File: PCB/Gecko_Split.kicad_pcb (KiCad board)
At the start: 2 copper layers, 142.5 x 106.3 mm, 83 parts, among them J1 LED, J2 4PIN, J3 OLED, P1 i2c_pin, P2 i2c_pin, SW1 SW_PUSH, SW10 SW_PUSH, SW11 SW_PUSH, SW12 SW_PUSH, SW13 SW_PUSH, SW14 SW_PUSH, SW15 SW_PUSH, SW16 SW_PUSH, SW17 SW_PUSH, SW18 SW_PUSH, SW19 SW_PUSH, SW2 SW_PUSH, SW20 SW_PUSH, SW21 SW_PUSH, SW22 SW_PUSH, SW23 SW_PUSH, SW24 SW_PUSH, SW25 SW_PUSH, SW26 SW_PUSH, SW27 SW_PUSH, SW28 SW_PUSH, SW29 SW_PUSH, SW3 SW_PUSH, SW4 SW_PUSH, SW5 SW_PUSH, SW6 SW_PUSH, SW7 SW_PUSH, SW8 SW_PUSH, SW9 SW_PUSH, U1 ProMicro

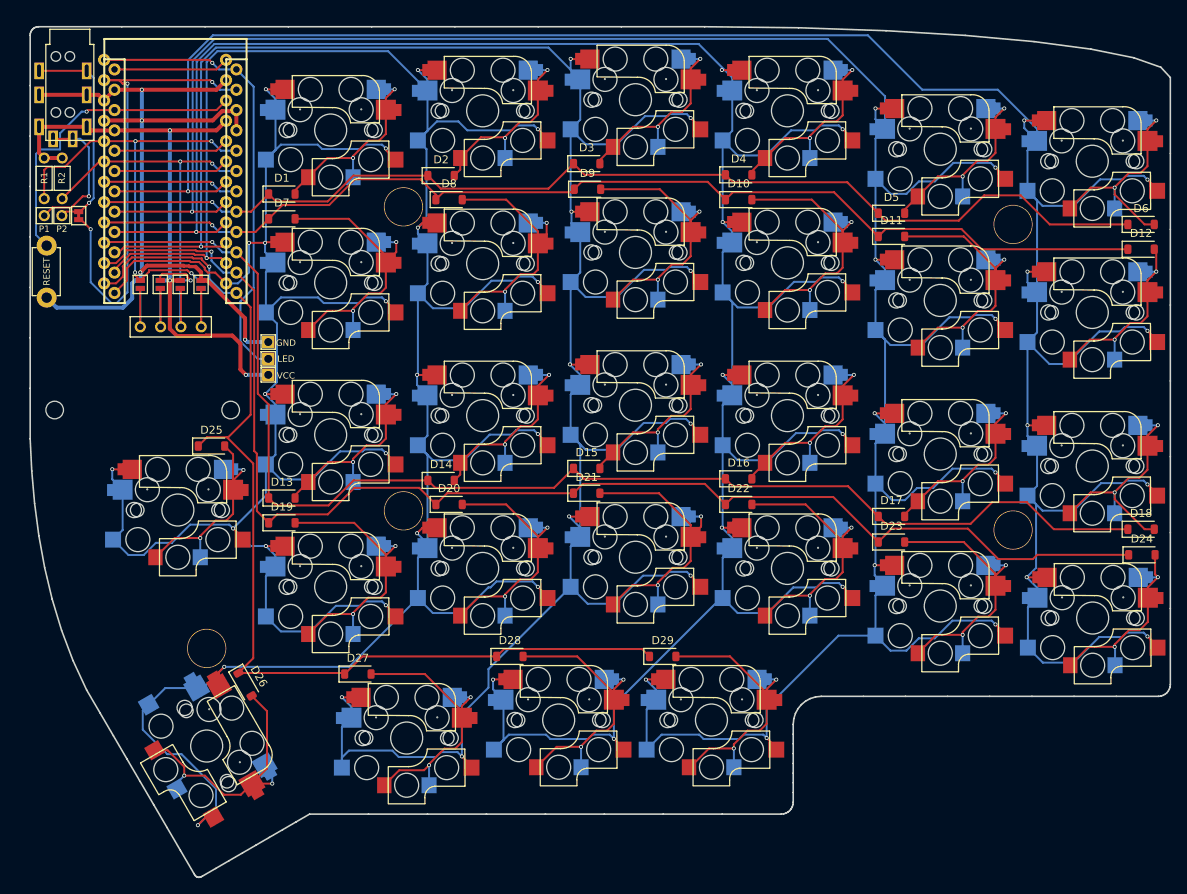
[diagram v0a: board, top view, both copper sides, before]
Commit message: add charging protection, LED and rotary encoder
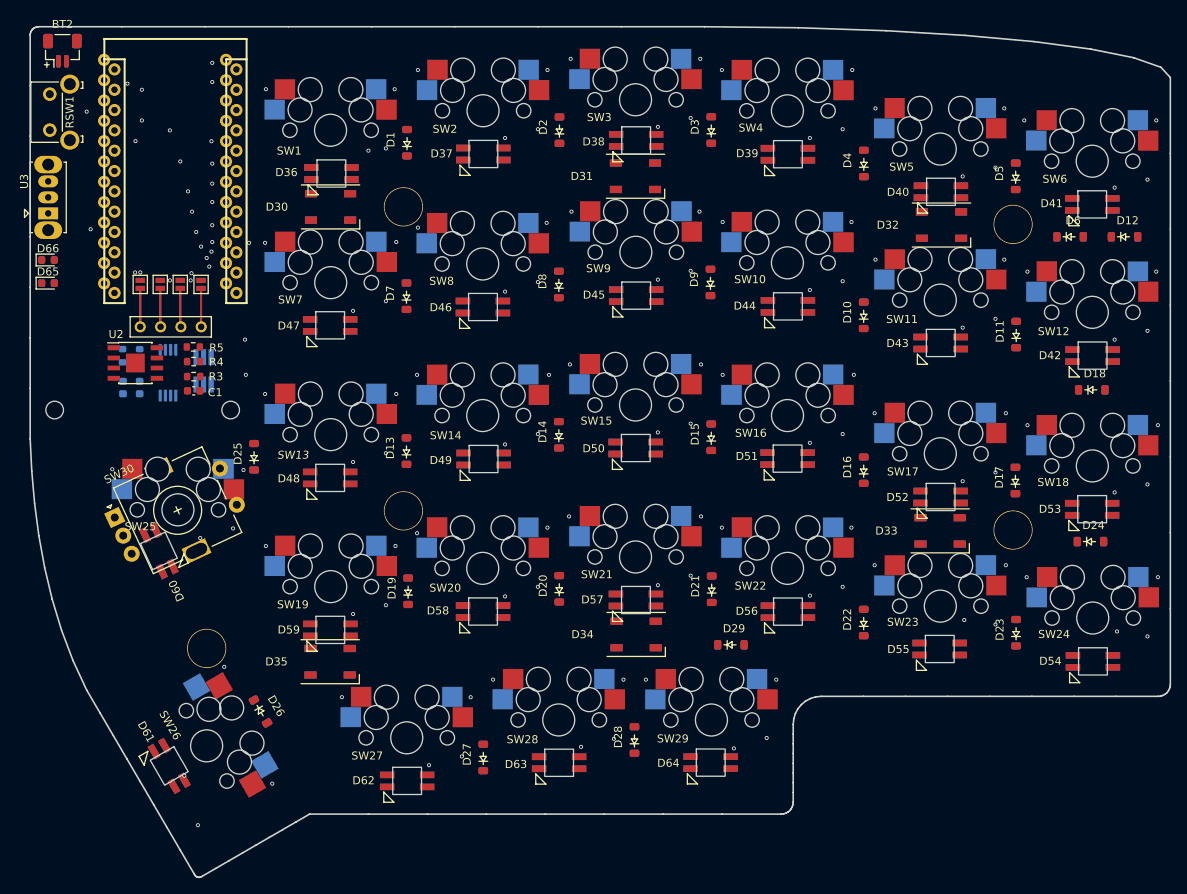
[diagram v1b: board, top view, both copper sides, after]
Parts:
- removed J1: LED, Lily58-footprint:LED
- removed the J2 at (87.9, 39.3)
- removed P1, P2: i2c_pin, Lily58-footprint:1pin_conn
- removed R1, R2: R, Lily58-footprint:RESISTOR_mini
- removed W1: jumper, Lily58-footprint:jumper_data
- added BT2: Battery_Cell, Connector_JST:JST_SH_BM02B-SRSS-TB_1x02-1MP_P1.00mm_Vertical, F.Cu at (87.0, 40.1)
- added C1: 0.1UF-25V-5%, Capacitor_SMD:C_0603_1608Metric, F.Cu at (103.4, 82.6)
- added C2: 0.1UF-25V-5%, Capacitor_SMD:C_0603_1608Metric, B.Cu at (96.6, 82.2)
- added C3: 10UF, Capacitor_SMD:C_0603_1608Metric, B.Cu at (94.5, 82.2)
- added D30: WS2812B, LED_SMD:LED_WS2812B_BothSides, F.Cu at (120.4, 59.6)
- added D31: WS2812B, LED_SMD:LED_WS2812B_BothSides, F.Cu at (158.5, 55.8)
- added D32: WS2812B, LED_SMD:LED_WS2812B_BothSides, F.Cu at (196.7, 61.9)
- added D33: WS2812B, LED_SMD:LED_WS2812B_BothSides, F.Cu at (196.6, 100.1)
- added D34: WS2812B, LED_SMD:LED_WS2812B_BothSides, F.Cu at (158.6, 113.1)
- added D35: WS2812B, LED_SMD:LED_WS2812B_BothSides, F.Cu at (120.3, 116.5)
- added D36: SK6812MINI, LED_SMD:LED_SK6812MINI_THROUGH, F.Cu at (120.6, 55.4)
- added D37: SK6812MINI, LED_SMD:LED_SK6812MINI_THROUGH, F.Cu at (139.6, 53.0)
- added D38: SK6812MINI, LED_SMD:LED_SK6812MINI_THROUGH, F.Cu at (158.7, 51.3)
- added D39: SK6812MINI, LED_SMD:LED_SK6812MINI_THROUGH, F.Cu at (177.7, 53.0)
- added D40: SK6812MINI, LED_SMD:LED_SK6812MINI_THROUGH, F.Cu at (196.8, 57.7)
- added D41: SK6812MINI, LED_SMD:LED_SK6812MINI_THROUGH, F.Cu at (215.7, 59.3)
- added D42: SK6812MINI, LED_SMD:LED_SK6812MINI_THROUGH, F.Cu at (215.7, 78.2)
- added D43: SK6812MINI, LED_SMD:LED_SK6812MINI_THROUGH, F.Cu at (196.8, 76.6)
- added D44: SK6812MINI, LED_SMD:LED_SK6812MINI_THROUGH, F.Cu at (177.7, 72.0)
- added D45: SK6812MINI, LED_SMD:LED_SK6812MINI_THROUGH, F.Cu at (158.7, 70.7)
- added D46: SK6812MINI, LED_SMD:LED_SK6812MINI_THROUGH, F.Cu at (139.5, 72.1)
- added D47: SK6812MINI, LED_SMD:LED_SK6812MINI_THROUGH, F.Cu at (120.4, 74.4)
- added D48: SK6812MINI, LED_SMD:LED_SK6812MINI_THROUGH, F.Cu at (120.4, 93.5)
- added D49: SK6812MINI, LED_SMD:LED_SK6812MINI_THROUGH, F.Cu at (139.6, 91.1)
- added D50: SK6812MINI, LED_SMD:LED_SK6812MINI_THROUGH, F.Cu at (158.6, 89.8)
- added D51: SK6812MINI, LED_SMD:LED_SK6812MINI_THROUGH, F.Cu at (177.6, 91.1)
- added D52: SK6812MINI, LED_SMD:LED_SK6812MINI_THROUGH, F.Cu at (196.7, 95.9)
- added D53: SK6812MINI, LED_SMD:LED_SK6812MINI_THROUGH, F.Cu at (215.7, 97.4)
- added D54: SK6812MINI, LED_SMD:LED_SK6812MINI_THROUGH, F.Cu at (215.8, 116.4)
- added D55: SK6812MINI, LED_SMD:LED_SK6812MINI_THROUGH, F.Cu at (196.6, 114.9)
- added D56: SK6812MINI, LED_SMD:LED_SK6812MINI_THROUGH, F.Cu at (177.7, 110.2)
- added D57: SK6812MINI, LED_SMD:LED_SK6812MINI_THROUGH, F.Cu at (158.7, 108.8)
- added D58: SK6812MINI, LED_SMD:LED_SK6812MINI_THROUGH, F.Cu at (139.5, 110.2)
- added D59: SK6812MINI, LED_SMD:LED_SK6812MINI_THROUGH, F.Cu at (120.5, 112.5)
- added D60: SK6812MINI, LED_SMD:LED_SK6812MINI_THROUGH, F.Cu at (99.0, 102.6)
- added D61: SK6812MINI, LED_SMD:LED_SK6812MINI_THROUGH, F.Cu at (100.3, 129.5)
- added D62: SK6812MINI, LED_SMD:LED_SK6812MINI_THROUGH, F.Cu at (130.1, 131.4)
- added D63: SK6812MINI, LED_SMD:LED_SK6812MINI_THROUGH, F.Cu at (149.1, 129.1)
- added D64: SK6812MINI, LED_SMD:LED_SK6812MINI_THROUGH, F.Cu at (168.0, 129.1)
- added D65: LED, LED_SMD:LED_0603_1608Metric, F.Cu at (85.2, 69.1)
- added D66: LED, LED_SMD:LED_0603_1608Metric, F.Cu at (85.2, 66.2)
- added IC1: DW01A, Package_TO_SOT_SMD:TSOT-23-6_HandSoldering, B.Cu at (104.6, 80.1)
- added Q1: FS8205A, Package_SO:TSSOP-8_4.4x3mm_P0.65mm, B.Cu at (100.2, 80.3)
- added R3: 1K OHM, Resistor_SMD:R_0603_1608Metric, F.Cu at (103.4, 80.8)
- added R4: 1K OHM, Resistor_SMD:R_0603_1608Metric, F.Cu at (103.4, 78.9)
- added R5: 1.2K Ohm, Resistor_SMD:R_0603_1608Metric, F.Cu at (103.3, 77.1)
- added R6: 100 OHM, Resistor_SMD:R_0603_1608Metric, B.Cu at (96.6, 78.2)
- added R7: 1K OHM, Resistor_SMD:R_0603_1608Metric, B.Cu at (94.5, 78.2)
- added SW30: RotaryEncoder_Switch, Rotary_Encoder:RotaryEncoder_Alps_EC11E-Switch_Vertical_H20mm, F.Cu at (93.5, 98.4)
- added U2: TP4056, KiCadCustomLibs-master:TP4056_SOIC-8, F.Cu at (96.1, 79.1)
- added U3: SK12D07VG4, Button_Switch_THT:SW_Slide_1P2T_CK_OS102011MS2Q, F.Cu at (85.2, 60.4)
- D1, D10, D11, D12, D13, D14, D15, D16, D17, D18, D19, D2, D20, D21, D22, D23, D24, D25, D26, D27, D28, D29, D3, D4, D5, D6, D7, D8, D9: footprint Diode_SMD:D_SOD-123 -> Diode_SMD:D_SOD-123-BothSides
- RSW1: footprint Lily58-footprint:TACT_SWITCH_TVBP06 -> Button_Switch_THT:SW_SPST_Omron_B3F-315x_Angled
- SW1, SW10, SW11, SW12, SW13, SW14, SW15, SW16, SW17, SW18, SW19, SW2, SW20, SW21, SW22, SW23, SW24, SW25, SW26, SW27, SW28, SW29, SW3, SW4, SW5, SW6, SW7, SW8, SW9: footprint Lily58_Pro-footprint:MX_Choc_Hotswap -> Lily58_Pro-footprint:MX_Socket_18mm
- moved D22 24.1 mm to (188.4, 114.0), turned to 90 degrees
- moved D10 23.9 mm to (188.4, 75.6), turned to 90 degrees
- moved D11 22.4 mm to (207.5, 78.0), turned to 90 degrees
- moved D21 22.2 mm to (169.4, 109.8), turned to 90 degrees
- moved D9 21.8 mm to (169.2, 71.5), turned to 90 degrees
- moved D23 21.7 mm to (207.4, 115.2), turned to 90 degrees
- moved D27 21.3 mm to (140.8, 130.8), turned to 90 degrees
- moved D28 21.2 mm to (159.7, 128.7), turned to 90 degrees
- moved D7 20.7 mm to (131.2, 73.2), turned to 90 degrees
- moved D19 20.3 mm to (131.5, 110.1), turned to 90 degrees
- moved D20 19.9 mm to (150.3, 109.8), turned to 90 degrees
- moved D8 19.9 mm to (150.3, 71.7), turned to 90 degrees
- moved D18 18.3 mm to (213.2, 83.7)
- moved RSW1 17.7 mm to (85.4, 50.0)
- moved D1 17.4 mm to (131.3, 54.0), turned to 90 degrees
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- renumbered J3 to J2
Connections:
- U1 pad 19: unconnected-(U1-A2(PF5)-Pad19) -> PADB
- U1 pad 2: DATA -> unconnected-(U1-RX(PD2)-Pad2)
- U1 pad 20: unconnected-(U1-A3(PF4)-Pad20) -> PADA
- U1 pad 24: unconnected-(U1-RAW-Pad24) -> BAT+
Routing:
- net col1: track 339.2 -> 0.00 mm
- net col2: track 318.5 -> 0.00 mm, vias 11 -> 9
- net col0: track 307.3 -> 0.00 mm, vias 9 -> 8
- net col3: track 306.7 -> 0.00 mm, vias 11 -> 10
- net col4: track 296.8 -> 0.00 mm
- net col5: track 219.9 -> 0.00 mm, vias 11 -> 10
- net row3: track 169.7 -> 0.00 mm
- net row2: track 165.3 -> 0.00 mm
- net row0: track 138.8 -> 0.00 mm
- net row1: track 138.6 -> 0.00 mm
- net row4: track 130.4 -> 0.00 mm
- net GND: track 105.5 -> 0.00 mm
- net VCC: track 74.4 -> 0.00 mm, vias 3 -> 4
- net DATA: track 61.1 -> 0.00 mm, vias 3 -> 0
- net LED: track 57.0 -> 0.00 mm
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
